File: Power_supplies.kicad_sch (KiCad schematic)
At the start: 38 parts, among them J2 DG35C-B-02P, T1 AOSP21357, T2 MJD32C, U3 MC34063, U4 MC34063, U5 TLV70233_SOT23-5

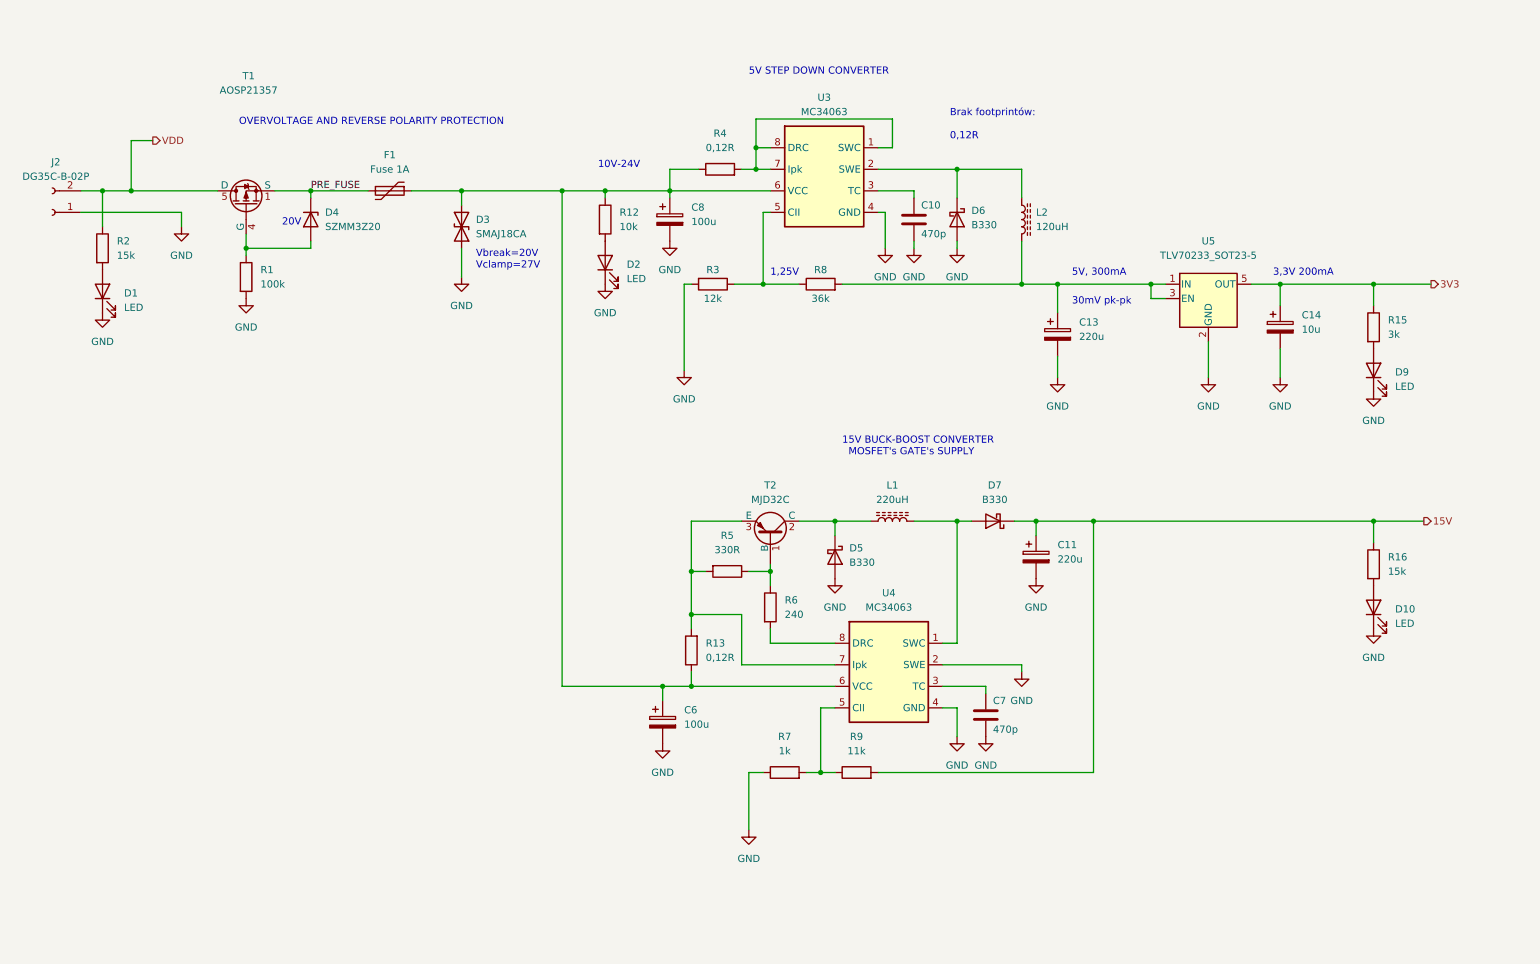
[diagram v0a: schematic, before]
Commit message: added power loss detection, preparing for new pcb layout
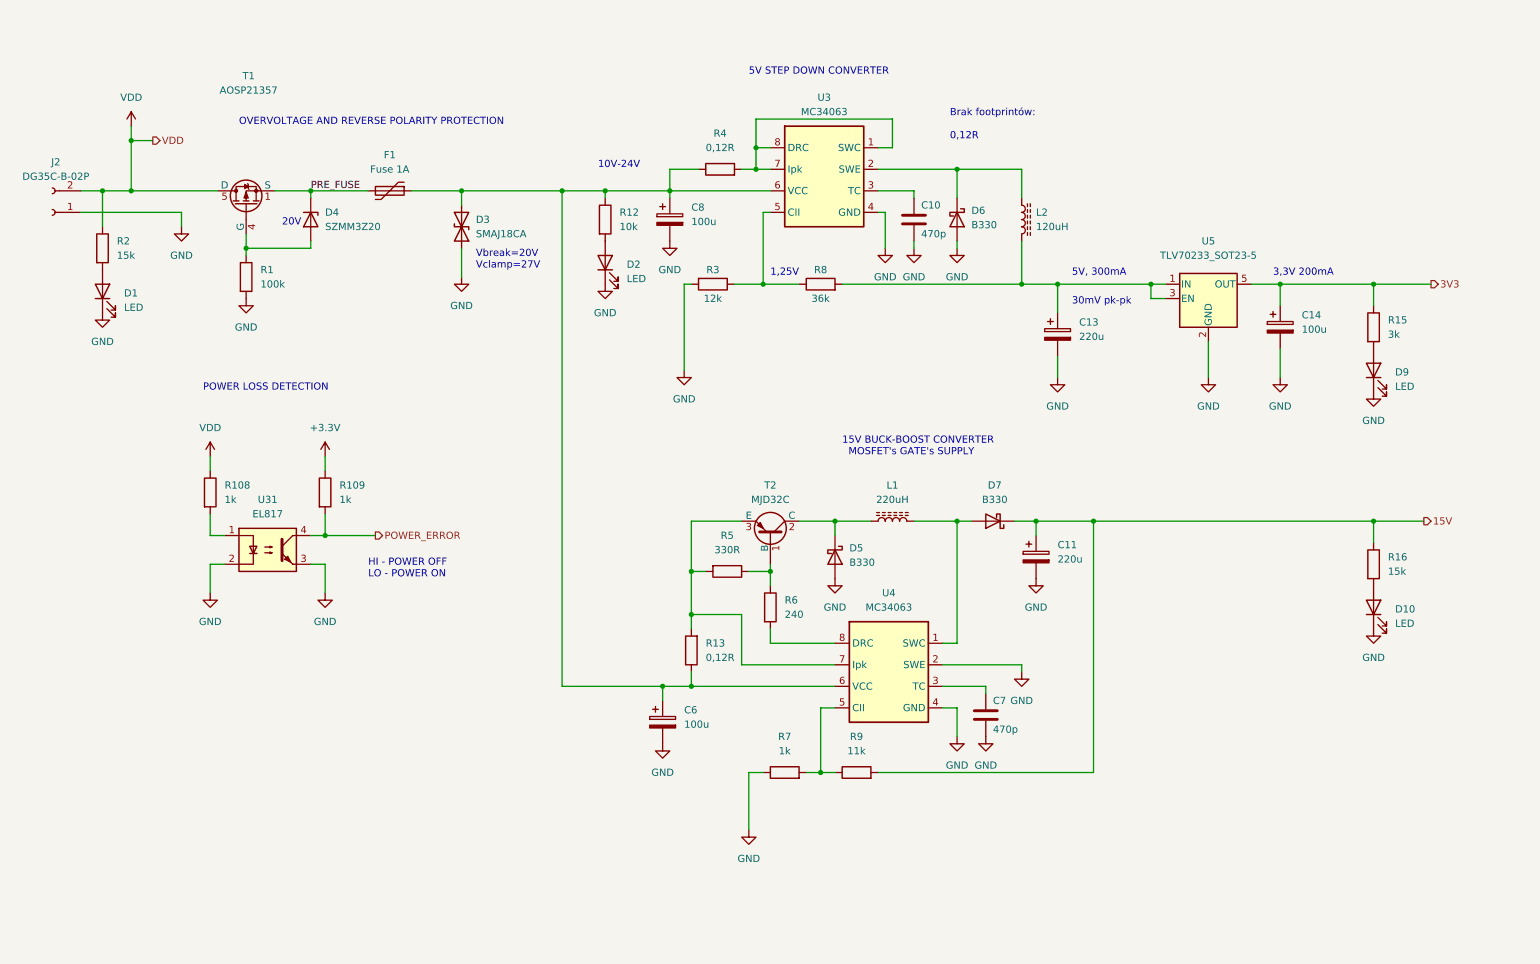
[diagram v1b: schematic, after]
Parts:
- added R108, R109: 1k, Resistor_SMD:R_0603_1608Metric, symbol Device:R
- added U31: EL817, Package_DIP:DIP-4_W7.62mm, symbol Isolator:EL817
- C14: value 10u -> 100u; footprint Capacitor_SMD:C_1206_3216Metric_Pad1.33x1.80mm_HandSolder -> Capacitor_SMD:CP_Elec_8x6.2
- D3: footprint Diode_SMD:D_SMA_Handsoldering -> Diode_THT:D_DO-201AE_P15.24mm_Horizontal
- D5, D6, D7: footprint Diode_SMD:D_SMA_Handsoldering -> Diode_SMD:D_SMC
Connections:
- net GND: now also U31.2, U31.3
- net VDD: now also R108.1
- new net: R108.2, U31.1
- new net +3V3: R109.1
- new net POWER_ERROR: R109.2, U31.4
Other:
- note added: "HI - POWER OFF LO - POWER ON"
- note added: "POWER LOSS DETECTION"

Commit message: pcb is in progress, finishing H-bridge layout
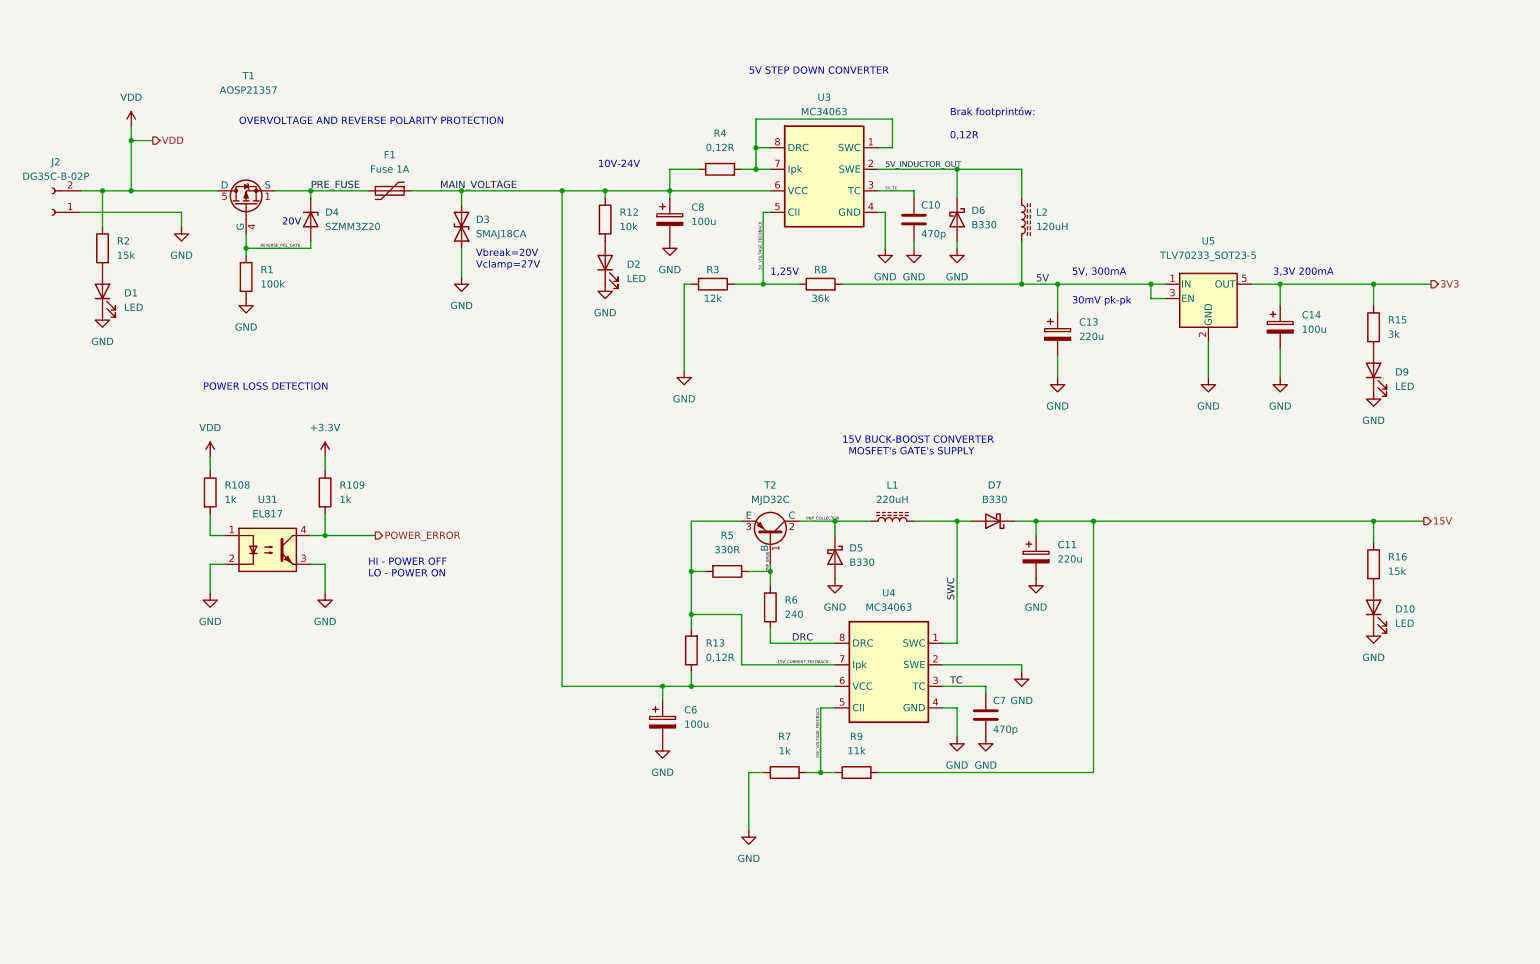
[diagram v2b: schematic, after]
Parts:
- C10, C7: footprint Capacitor_SMD:C_0603_1608Metric -> Capacitor_SMD:C_0603_1608Metric_Pad1.08x0.95mm_HandSolder
- D3: footprint Diode_THT:D_DO-201AE_P15.24mm_Horizontal -> Diode_SMD:D_SMA_Handsoldering
- D5, D6, D7: footprint Diode_SMD:D_SMC -> Diode_SMD:D_SMA_Handsoldering
- R1, R108, R109, R12, R15, R16, R2, R3, R5, R6, R7, R8, R9: footprint Resistor_SMD:R_0603_1608Metric -> Resistor_SMD:R_0603_1608Metric_Pad0.98x0.95mm_HandSolder
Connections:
- net 5V_INDUCTOR_OUT: now reaches D6.1 (K), L2.1, U3.2 (SWE)
- net 5V: now reaches C13.1, L2.2, R8.2, U5.1 (IN), U5.3 (EN)
- net MAIN_VOLTAGE: now reaches C6.1, C8.1, D3.2 (A2), F1.1, R12.1, R13.1, R4.1, U3.6 (VCC), U4.6 (VCC)
- net 5V_VOLTAGE_FEEDBACK: now reaches R3.1, R8.1, U3.5 (CII)
- net REVERSE_POL_GATE: now reaches D4.2 (A), R1.1, T1.4 (G)
- net SWC: now reaches D7.2 (A), L1.2, U4.1 (SWC)
- net TC: now reaches C7.1, U4.3 (TC)
- net 15V_VOLTAGE_FEEDBACK: now reaches R7.2, R9.1, U4.5 (CII)
- net 15V_CURRENT_FEEDBACK: now reaches R13.2, R5.2, T2.3 (E), U4.7 (Ipk)
- net DRC: now reaches R6.2, U4.8 (DRC)
- net PNP_COLLECTOR: now reaches D5.1 (K), L1.1, T2.2 (C)
- net 5V_TC: now reaches C10.1, U3.3 (TC)
- net PNP_BASE: now reaches R5.1, R6.1, T2.1 (B)
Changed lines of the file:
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@@
     (effects (font (size 1.27 1.27)) (justify left bottom))
+  )
+  (label "5V_INDUCTOR_OUT" (at 170.18 41.91 0)
+    (effects (font (size 1 1)) (justify left bottom))
+  )
+  (label "TC" (at 181.61 133.35 0)
+    (effects (font (size 1.27 1.27)) (justify left bottom))
+  )
+  (label "15V_VOLTAGE_FEEDBACK" (at 158.75 146.05 90)
+    (effects (font (size 0.5 0.5)) (justify left bottom))
+  )
+  (label "5V" (at 196.85 62.23 0)
+    (effects (font (size 1.27 1.27)) (justify left bottom))
+  )
+  (label "MAIN_VOLTAGE" (at 91.44 45.72 0)
+    (effects (font (size 1.27 1.27)) (justify left bottom))
+  )
+  (label "SWC" (at 182.88 118.11 90)
+    (effects (font (size 1.27 1.27)) (justify left bottom))
+  )
+  (label "REVERSE_POL_GATE" (at 59.69 55.88 0)
+    (effects (font (size 0.5 0.5)) (justify left bottom))
+  )
+  (label "PNP_BASE" (at 149.86 113.03 90)
+    (effects (font (size 0.5 0.5)) (justify left bottom))
+  )
+  (label "15V_CURRENT_FEEDBACK" (at 151.13 129.54 0)
+    (effects (font (size 0.5 0.5)) (justify left bottom))
+  )
+  (label "DRC" (at 153.67 125.73 0)
+    (effects (font (size 1.27 1.27)) (justify left bottom))
+  )
+  (label "5V_TC" (at 170.18 45.72 0)
+    (effects (font (size 0.5 0.5)) (justify left bottom))
+  )
+  (label "5V_VOLTAGE_FEEDBACK" (at 148.59 59.69 90)
+    (effects (font (size 0.5 0.5)) (justify left bottom))
+  )
+  (label "PNP_COLLECTOR" (at 156.21 104.14 0)
+    (effects (font (size 0.5 0.5)) (justify left bottom))
   )
   (label "PRE_FUSE" (at 68.58 45.72 0)
@@
       (effects (font (size 1.27 1.27)) (justify left))
     )
-    (property "Footprint" "Resistor_SMD:R_0603_1608Metric" (id 2) (at 49.022 99.06 90)
+    (property "Footprint" "Resistor_SMD:R_0603_1608Metric_Pad0.98x0.95mm_HandSolder" (id 2) (at 49.022 99.06 90)
       (effects (font (size 1.27 1.27)) hide)
     )
@@
       (effects (font (size 1.27 1.27)) (justify right))
     )
-    (property "Footprint" "Diode_THT:D_DO-201AE_P15.24mm_Horizontal" (id 2) (at 100.33 52.07 0)
+    (property "Footprint" "Diode_SMD:D_SMA_Handsoldering" (id 2) (at 100.33 52.07 0)
       (effects (font (size 1.27 1.27)) hide)
     )
@@
     (property "Reference" "R3" (id 0) (at 139.7 59.69 90))
     (property "Value" "12k" (id 1) (at 139.7 64.77 90))
-    (property "Footprint" "Resistor_SMD:R_0603_1608Metric" (id 2) (at 139.7 60.452 90)
+    (property "Footprint" "Resistor_SMD:R_0603_1608Metric_Pad0.98x0.95mm_HandSolder" (id 2) (at 139.7 60.452 90)
       (effects (font (size 1.27 1.27)) hide)
     )
@@
       (effects (font (size 1.27 1.27)) (justify left))
     )
-    (property "Footprint" "Resistor_SMD:R_0603_1608Metric" (id 2) (at 55.372 60.96 90)
+    (property "Footprint" "Resistor_SMD:R_0603_1608Metric_Pad0.98x0.95mm_HandSolder" (id 2) (at 55.372 60.96 90)
       (effects (font (size 1.27 1.27)) hide)
     )
@@
       (effects (font (size 1.27 1.27)) (justify left))
     )
-    (property "Footprint" "Resistor_SMD:R_0603_1608Metric" (id 2) (at 69.342 99.06 90)
+    (property "Footprint" "Resistor_SMD:R_0603_1608Metric_Pad0.98x0.95mm_HandSolder" (id 2) (at 69.342 99.06 90)
       (effects (font (size 1.27 1.27)) hide)
     )
@@
       (effects (font (size 1.27 1.27)) (justify left))
     )
-    (property "Footprint" "Resistor_SMD:R_0603_1608Metric" (id 2) (at 29.972 55.88 90)
+    (property "Footprint" "Resistor_SMD:R_0603_1608Metric_Pad0.98x0.95mm_HandSolder" (id 2) (at 29.972 55.88 90)
       (effects (font (size 1.27 1.27)) hide)
     )
@@
       (effects (font (size 1.27 1.27)) (justify left))
     )
-    (property "Footprint" "Diode_SMD:D_SMC" (id 2) (at 156.845 110.49 0)
+    (property "Footprint" "Diode_SMD:D_SMA_Handsoldering" (id 2) (at 156.845 110.49 0)
       (effects (font (size 1.27 1.27)) hide)
     )
@@
       (effects (font (size 1.27 1.27)) (justify left))
     )
-    (property "Footprint" "Capacitor_SMD:C_0603_1608Metric" (id 2) (at 176.2252 54.61 0)
+    (property "Footprint" "Capacitor_SMD:C_0603_1608Metric_Pad1.08x0.95mm_HandSolder" (id 2) (at 176.2252 54.61 0)
       (effects (font (size 1.27 1.27)) hide)
     )
@@
     (property "Reference" "R5" (id 0) (at 142.24 106.68 90))
     (property "Value" "330R" (id 1) (at 142.24 109.22 90))
-    (property "Footprint" "Resistor_SMD:R_0603_1608Metric" (id 2) (at 142.24 111.252 90)
+    (property "Footprint" "Resistor_SMD:R_0603_1608Metric_Pad0.98x0.95mm_HandSolder" (id 2) (at 142.24 111.252 90)
       (effects (font (size 1.27 1.27)) hide)
     )
@@
       (effects (font (size 1.27 1.27)) (justify left))
     )
-    (property "Footprint" "Resistor_SMD:R_0603_1608Metric" (id 2) (at 254.762 69.85 90)
+    (property "Footprint" "Resistor_SMD:R_0603_1608Metric_Pad0.98x0.95mm_HandSolder" (id 2) (at 254.762 69.85 90)
       (effects (font (size 1.27 1.27)) hide)
     )
@@
       (effects (font (size 1.27 1.27)) (justify left))
     )
-    (property "Footprint" "Capacitor_SMD:C_0603_1608Metric" (id 2) (at 188.9252 142.24 0)
+    (property "Footprint" "Capacitor_SMD:C_0603_1608Metric_Pad1.08x0.95mm_HandSolder" (id 2) (at 188.9252 142.24 0)
       (effects (font (size 1.27 1.27)) hide)
     )
@@
       (effects (font (size 1.27 1.27)) (justify left))
     )
-    (property "Footprint" "Resistor_SMD:R_0603_1608Metric" (id 2) (at 148.082 119.38 90)
+    (property "Footprint" "Resistor_SMD:R_0603_1608Metric_Pad0.98x0.95mm_HandSolder" (id 2) (at 148.082 119.38 90)
       (effects (font (size 1.27 1.27)) hide)
     )
@@
     (property "Reference" "R7" (id 0) (at 152.4 142.24 90))
     (property "Value" "1k" (id 1) (at 152.4 144.78 90))
-    (property "Footprint" "Resistor_SMD:R_0603_1608Metric" (id 2) (at 152.4 150.368 90)
+    (property "Footprint" "Resistor_SMD:R_0603_1608Metric_Pad0.98x0.95mm_HandSolder" (id 2) (at 152.4 150.368 90)
       (effects (font (size 1.27 1.27)) hide)
     )
@@
     (property "Reference" "R9" (id 0) (at 165.1 142.24 90))
     (property "Value" "11k" (id 1) (at 165.1 144.78 90))
-    (property "Footprint" "Resistor_SMD:R_0603_1608Metric" (id 2) (at 165.1 150.368 90)
+    (property "Footprint" "Resistor_SMD:R_0603_1608Metric_Pad0.98x0.95mm_HandSolder" (id 2) (at 165.1 150.368 90)
       (effects (font (size 1.27 1.27)) hide)
     )
@@
       (effects (font (size 1.27 1.27)) (justify left))
     )
-    (property "Footprint" "Resistor_SMD:R_0603_1608Metric" (id 2) (at 118.872 50.8 90)
+    (property "Footprint" "Resistor_SMD:R_0603_1608Metric_Pad0.98x0.95mm_HandSolder" (id 2) (at 118.872 50.8 90)
       (effects (font (size 1.27 1.27)) hide)
     )
@@
     (property "Reference" "D7" (id 0) (at 189.5475 97.79 0))
     (property "Value" "B330" (id 1) (at 189.5475 100.33 0))
-    (property "Footprint" "Diode_SMD:D_SMC" (id 2) (at 189.23 99.695 0)
+    (property "Footprint" "Diode_SMD:D_SMA_Handsoldering" (id 2) (at 189.23 99.695 0)
       (effects (font (size 1.27 1.27)) hide)
     )
@@
     (property "Reference" "R8" (id 0) (at 158.75 59.69 90))
     (property "Value" "36k" (id 1) (at 158.75 64.77 90))
-    (property "Footprint" "Resistor_SMD:R_0603_1608Metric" (id 2) (at 158.75 64.008 90)
+    (property "Footprint" "Resistor_SMD:R_0603_1608Metric_Pad0.98x0.95mm_HandSolder" (id 2) (at 158.75 64.008 90)
       (effects (font (size 1.27 1.27)) hide)
     )
@@
       (effects (font (size 1.27 1.27)) (justify left))
     )
-    (property "Footprint" "Diode_SMD:D_SMC" (id 2) (at 178.435 50.8 0)
+    (property "Footprint" "Diode_SMD:D_SMA_Handsoldering" (id 2) (at 178.435 50.8 0)
       (effects (font (size 1.27 1.27)) hide)
     )
@@
       (effects (font (size 1.27 1.27)) (justify left))
     )
-    (property "Footprint" "Resistor_SMD:R_0603_1608Metric" (id 2) (at 254.762 111.76 90)
-      (effects (font (size 1.27 1.27)) hide)
-    )
+    (property "Footprint" "Resistor_SMD:R_0603_1608Metric_Pad0.98x0.95mm_HandSolder" (id 2) (at 254.762 111.76 90)
+      (effects (font (size 1.27 1.27)) hide)
+    )

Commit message: start design power input
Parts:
- U31: footprint Package_DIP:DIP-4_W7.62mm -> Package_DIP:DIP-4_W8.89mm_SMDSocket_LongPads
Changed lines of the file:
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@@
     (property "Reference" "U31" (id 0) (at 60.96 100.33 0))
     (property "Value" "EL817" (id 1) (at 60.96 102.87 0))
-    (property "Footprint" "Package_DIP:DIP-4_W7.62mm" (id 2) (at 55.88 114.3 0)
+    (property "Footprint" "Package_DIP:DIP-4_W8.89mm_SMDSocket_LongPads" (id 2) (at 55.88 114.3 0)
       (effects (font (size 1.27 1.27) italic) (justify left) hide)
     )

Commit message: ADC resistors and outputs added
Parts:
- added TP1, TP16, TP17, TP25, TP32, TP33, TP40, TP41, TP48, TP8, TP9, TP93, TP94: TestPoint, TestPoint:TestPoint_THTPad_1.0x1.0mm_Drill0.5mm, symbol Connector:TestPoint
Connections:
- net 15V: now also TP94.1
- net 3V3: now also TP25.1
- net 5V_VOLTAGE_FEEDBACK: now also TP17.1
- net GND: now also TP32.1, TP33.1, TP40.1, TP41.1, TP48.1
- net MAIN_VOLTAGE: now also TP16.1
- net POWER_ERROR: now also TP9.1
- net PRE_FUSE: now also TP8.1
- net VDD: now also TP1.1
- net at R108.2, U31.1: now also TP93.1

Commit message: project finished before changes
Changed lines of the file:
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@@
   (junction (at 135.89 113.03) (diameter 0) (color 0 0 0 0)
   )
+  (junction (at 90.17 45.72) (diameter 0) (color 0 0 0 0)
+  )
   (junction (at 149.86 113.03) (diameter 0) (color 0 0 0 0)
   )
@@
     (stroke (width 0) (type default) (color 0 0 0 0))
   )
+  (wire (pts (xy 90.17 45.72) (xy 95.25 45.72))
+    (stroke (width 0) (type default) (color 0 0 0 0))
+  )
   (wire (pts (xy 256.54 100.33) (xy 256.54 104.14))
     (stroke (width 0) (type default) (color 0 0 0 0))
@@
     (stroke (width 0) (type default) (color 0 0 0 0))
   )
+  (wire (pts (xy 93.98 38.1) (xy 90.17 38.1))
+    (stroke (width 0) (type default) (color 0 0 0 0))
+  )
   (wire (pts (xy 134.62 77.47) (xy 134.62 62.23))
     (stroke (width 0) (type default) (color 0 0 0 0))
@@
     (stroke (width 0) (type default) (color 0 0 0 0))
   )
+  (wire (pts (xy 90.17 38.1) (xy 90.17 45.72))
+    (stroke (width 0) (type default) (color 0 0 0 0))
+  )
   (wire (pts (xy 135.89 130.81) (xy 135.89 133.35))
     (stroke (width 0) (type default) (color 0 0 0 0))
@@
     (stroke (width 0) (type default) (color 0 0 0 0))
   )
-  (wire (pts (xy 86.36 45.72) (xy 95.25 45.72))
+  (wire (pts (xy 86.36 45.72) (xy 90.17 45.72))
     (stroke (width 0) (type default) (color 0 0 0 0))
   )
@@
     (effects (font (size 1.27 1.27)) (justify left bottom))
   )
+  (hierarchical_label "MAIN_VOLTAGE" (shape passive) (at 93.98 38.1 0)
+    (effects (font (size 1.27 1.27)) (justify left))
+  )
   (hierarchical_label "3V3" (shape output) (at 266.7 62.23 0)
